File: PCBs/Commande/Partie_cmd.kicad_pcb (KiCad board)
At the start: 4 copper layers, 85 x 82 mm, 54 parts, among them J2 UltraB, J3 UltraF, J4 Audio, J5 Acc, J6 M1, J7 M2, J8 TOF, J9 694106105102, U1 ESP32-S3-DEVKITC-1-N8R2, U2 BU18SD5WG-TL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

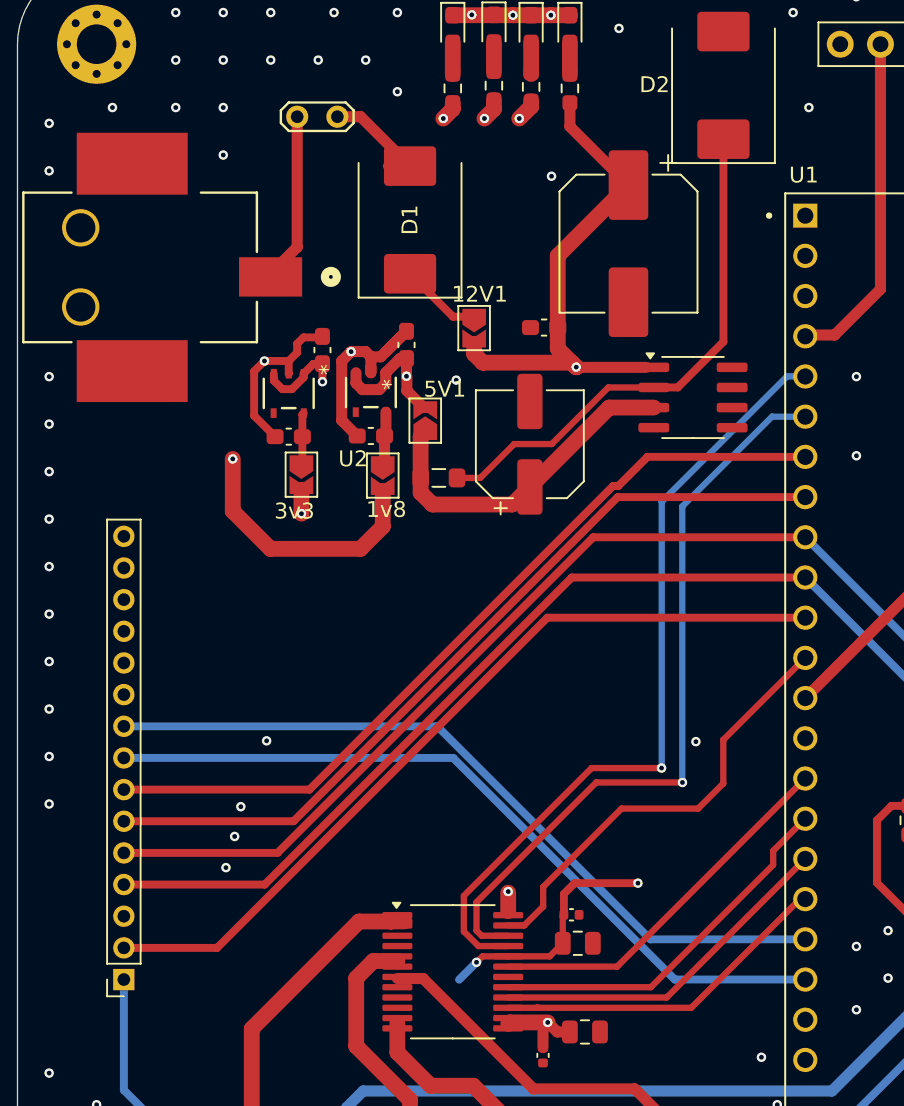
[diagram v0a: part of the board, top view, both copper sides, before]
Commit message: edit 3v3 zone
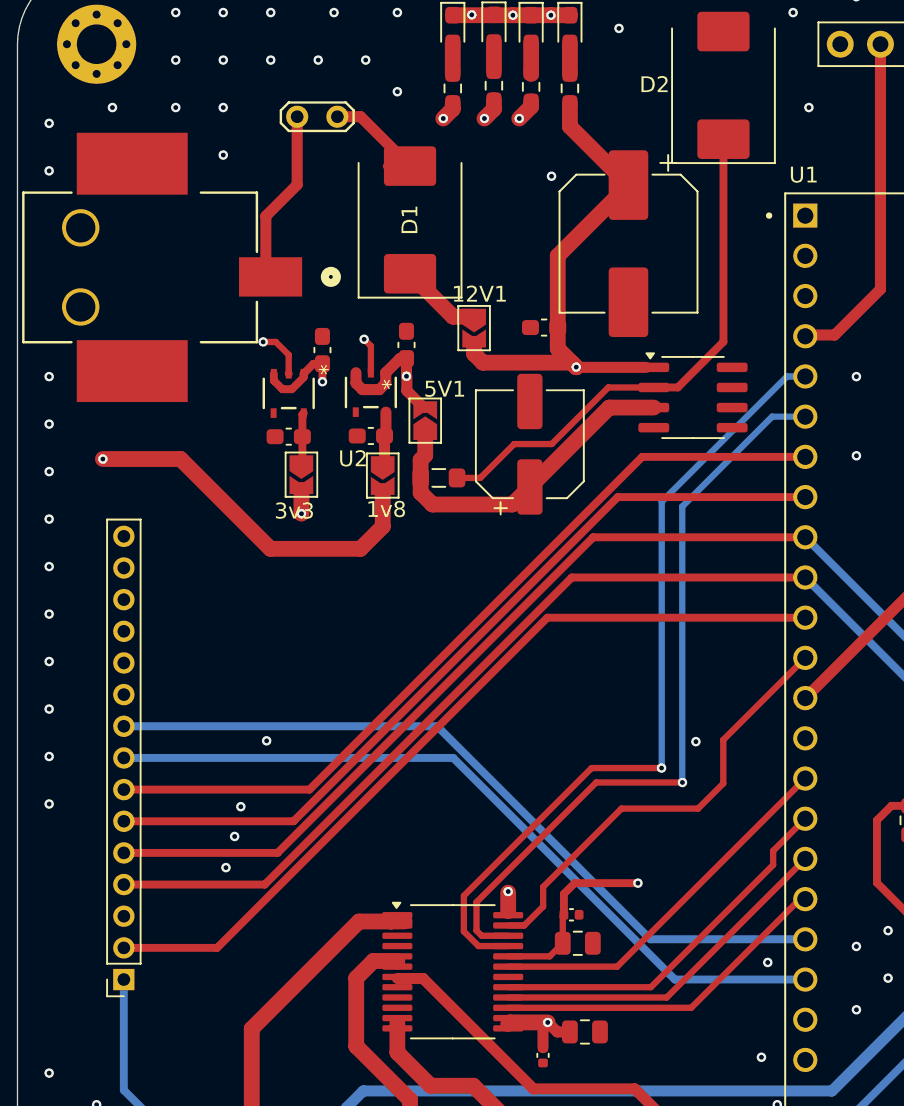
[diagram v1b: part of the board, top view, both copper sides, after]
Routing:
- net 3.3V: track 234.5 -> 282.5 mm, vias 5 -> 4
- net GND: track 34.6 -> 15.5 mm
- net 5V: track 170.3 -> 176.8 mm
- net 1.8V: track 83.5 -> 86.1 mm
- removed copper zone on In1.Cu, net 3.3V

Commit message: Last pcbss
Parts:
- C6: value 105n -> 1u
- moved C1 1.16 mm to (136.1, 103.3)
- moved C2 0.30 mm to (135.7, 104.8)
- turned C3 to 0 degrees
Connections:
- J4 pad 15: 3.3V -> unconnected-(J4-Pin_15-Pad15)
- J4 pad 3: 1.8V -> 3.3V
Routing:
- net 12V: track 183.8 -> 34.4 mm
- net 5V: track 176.8 -> 40.6 mm
- net 1.8V: track 86.1 -> 30.1 mm
- net 3.3V: track 282.5 -> 264.6 mm
- net AIN2: track 47.6 -> 44.4 mm
- net GND: track 15.5 -> 18.1 mm, vias 95 -> 111
- net AIN1: track 50.4 -> 47.9 mm
- net PWMA: track 28.1 -> 26.8 mm
- net Net-(D2-K): track 33.7 -> 34.9 mm
- net BIN1: track 23.7 -> 23.2 mm
- added copper zone on In1.Cu, net 12V
- added copper zone on In1.Cu, net 5V
- removed copper zone on In1.Cu, net GND

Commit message: Finitions pcb
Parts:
- moved D11 18.3 mm to (180.8, 90.0), turned to -90 degrees
- moved D10 18.2 mm to (180.8, 86.3), turned to 90 degrees
- moved D9 18.1 mm to (180.8, 82.8), turned to -90 degrees
- moved D8 18.1 mm to (180.8, 79.2), turned to 90 degrees
- moved R3 11.7 mm to (178.3, 80.0), turned to 0 degrees
- moved R2 11.5 mm to (178.2, 78.2), turned to 0 degrees
- moved R6 11.3 mm to (178.0, 84.0), turned to 0 degrees
- moved R7 11.3 mm to (178.0, 86.8), turned to 0 degrees
- moved C6 4.96 mm to (138.0, 67.4), turned to 90 degrees
- moved C3 0.40 mm to (138.6, 61.0)
- moved R9 0.13 mm to (156.2, 96.9)
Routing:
- net GND: track 18.1 -> 35.7 mm, vias 111 -> 115
- net 12V: track 34.4 -> 29.6 mm, vias 3 -> 4
- net Net-(U1-GPIO36): track 7.30 -> 2.73 mm
- net Net-(U1-GPIO37): track 7.32 -> 2.87 mm
- net Net-(U1-MTCK/GPIO39): track 7.77 -> 3.58 mm
- net Net-(U1-GPIO38): track 7.23 -> 3.46 mm
- net Net-(D11-A): track 2.18 -> 4.86 mm
- net Net-(D9-A): track 2.18 -> 4.34 mm
- net AIN1: track 47.9 -> 48.9 mm
- net Net-(D10-A): track 2.18 -> 2.88 mm
- net SDA: track 163.5 -> 164.1 mm
- net AIN2: track 44.4 -> 45.0 mm
- added copper zone on In1.Cu, net 3.3V
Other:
- board text added: "B"
- board text added: "T"
